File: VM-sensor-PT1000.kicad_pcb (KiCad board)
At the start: 2 copper layers, 25.4 x 19 mm, 15 parts, among them P1 PT100, P2 CONN_01X03, U1 AMS1117, U2 MCP6001

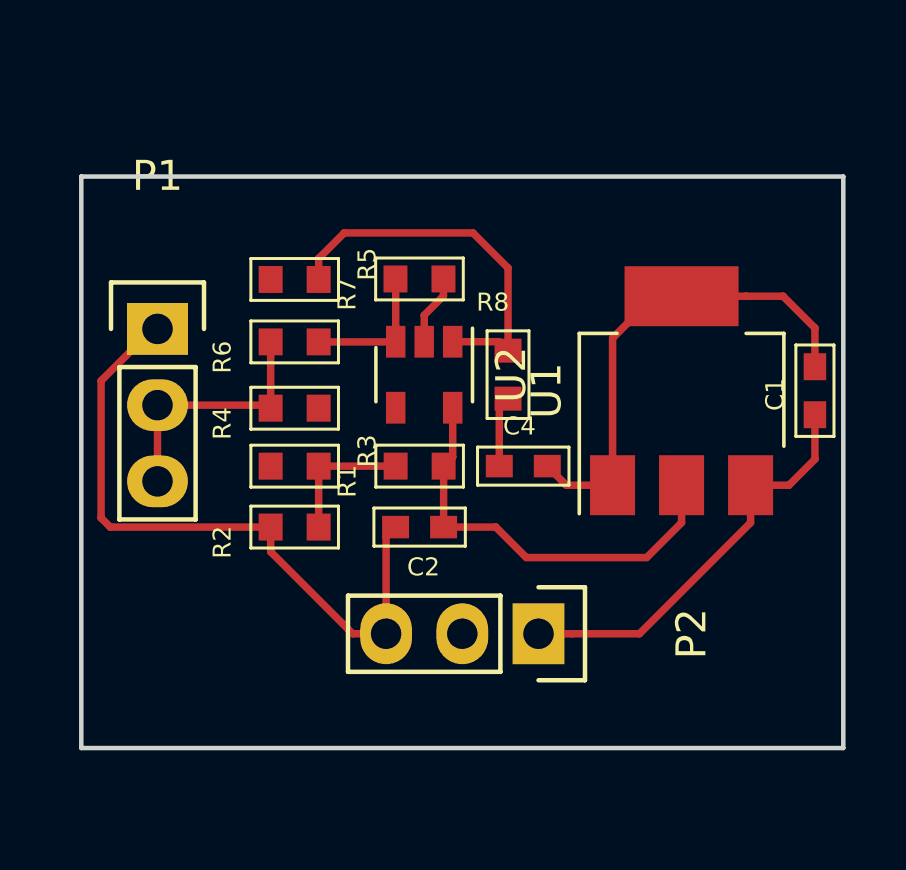
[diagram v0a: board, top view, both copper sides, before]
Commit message: change component 0603 to 0805 & header
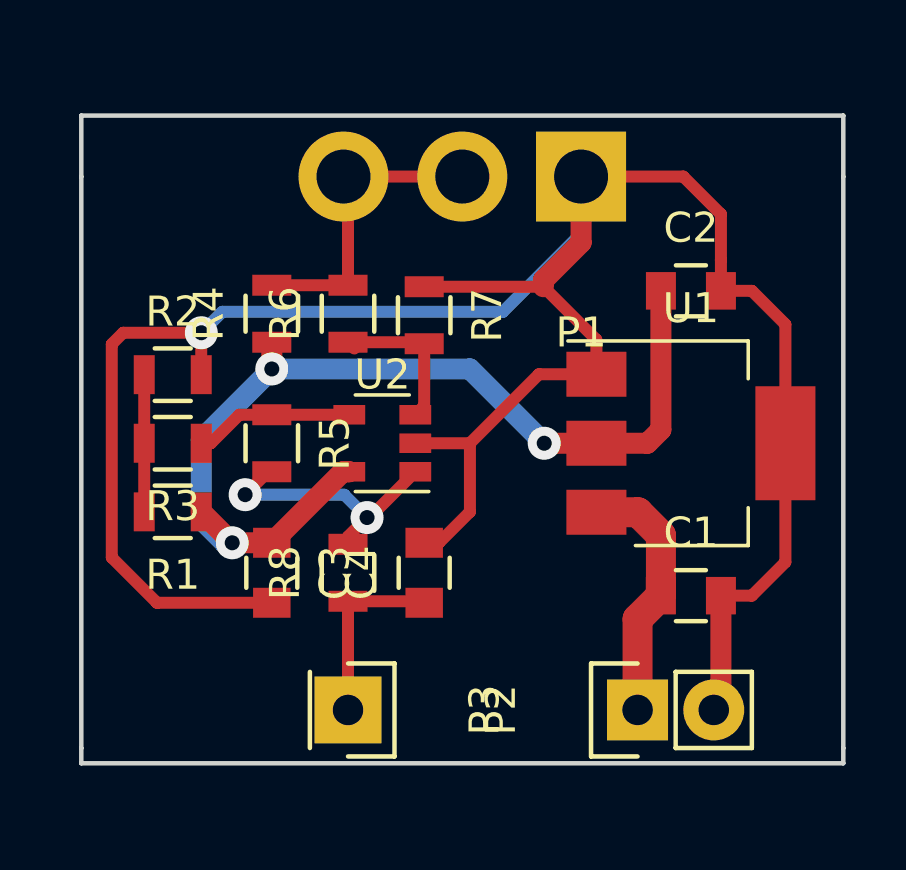
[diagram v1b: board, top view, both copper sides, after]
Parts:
- added C3: lib:C_0603, Capacitors_SMD:C_0805, F.Cu at (120.7, 76.7)
- added P3: PWR, Pin_Headers:Pin_Header_Straight_1x02, F.Cu at (132.8, 81.3)
- C1, C2, C4: footprint lib:C_0603 -> Capacitors_SMD:C_0805
- P1: footprint Pin_Headers:Pin_Header_Straight_1x03 -> Connectors_Hirose:Hirose_DF63-3P-3.96DSA_03x3.96mm_Straight
- P2: value CONN_01X03 -> ADC; footprint Pin_Headers:Pin_Header_Straight_1x03 -> Pin_Headers:Pin_Header_Straight_1x01
- R1, R2, R3, R4, R5, R6, R7, R8: footprint lib:R_0603 -> Resistors_SMD:R_0805
- moved P1 15.0 mm to (131.0, 63.5), turned to 180 degrees
- moved C2 12.0 mm to (134.6, 67.3), turned to 0 degrees
- moved R8 8.49 mm to (123.2, 76.7)
- moved R1 8.37 mm to (117.3, 74.7)
- moved C1 7.99 mm to (134.6, 77.5), turned to 0 degrees
- moved P2 6.84 mm to (123.2, 81.3)
- moved R2 6.51 mm to (117.3, 70.1), turned to 0 degrees
- moved R5 5.51 mm to (120.7, 72.4), turned to 270 degrees
- moved C4 4.85 mm to (125.7, 76.7), turned to 90 degrees
- moved R3 4.14 mm to (117.3, 72.4), turned to 180 degrees
- moved R4 3.24 mm to (120.7, 68.1), turned to 90 degrees
- moved U2 2.68 mm to (124.3, 72.4), turned to 180 degrees
- moved R6 2.01 mm to (123.2, 68.1), turned to 90 degrees
- moved U1 1.78 mm to (134.6, 72.4), turned to 0 degrees
- moved R7 1.22 mm to (125.7, 68.1), turned to 270 degrees
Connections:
- P2 pad 1: VCC -> /ADC
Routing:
- net GND: track 41.2 -> 81.6 mm, vias 0 -> 1
- net +3V3: track 14.2 -> 33.4 mm, vias 0 -> 3
- net Net-(R3-Pad1): track 0.00 -> 5.33 mm
- net VCC: track 13.8 -> 8.61 mm
- net /ADC: track 2.37 -> 6.18 mm
- net Net-(R5-Pad2): track 12.6 -> 8.98 mm, vias 0 -> 2
- net /Red: track 8.56 -> 10.2 mm
- net Net-(R6-Pad1): track 4.67 -> 5.35 mm
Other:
- board size 25.4 x 19 mm -> 25.4 x 21.6 mm
- net class Default: trace_width 0.25 -> 0.4; via_dia 0.8 -> 1.1; via_drill 0.4 -> 0.5

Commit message: Completed PCB
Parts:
- added REF**: SolderWirePad_single_1-2mmDrill, Wire_Pads:SolderWirePad_single_1-2mmDrill, F.Cu at (116.6, 63.0)
- added REF**: SolderWirePad_single_1-2mmDrill, Wire_Pads:SolderWirePad_single_1-2mmDrill, F.Cu at (116.6, 81.3)
- added REF**: SolderWirePad_single_1-2mmDrill, Wire_Pads:SolderWirePad_single_1-2mmDrill, F.Cu at (136.9, 62.7)
- moved R2 4.78 mm to (116.5, 74.8)
- moved R1 2.45 mm to (116.5, 72.4)
- moved R3 2.45 mm to (116.5, 70.1)
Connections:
- net /Red renamed /Blue
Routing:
- net +3V3: track 33.4 -> 55.9 mm, vias 3 -> 0
- net GND: track 81.6 -> 68.1 mm, vias 1 -> 0
- net Net-(R5-Pad2): track 8.98 -> 7.27 mm, vias 2 -> 0
- net Net-(R3-Pad1): track 5.33 -> 6.38 mm
- added copper zone on F.Cu, net GND
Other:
- board size 25.4 x 21.6 mm -> 26 x 24.8 mm
- net class Default: trace_width 0.4 -> 0.7
- board text added: "ADC"
- board text added: "Blue"
- board text added: "GND"
- board text added: "Red"
- board text added: "VCC"
